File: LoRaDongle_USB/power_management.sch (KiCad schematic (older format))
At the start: 15 parts

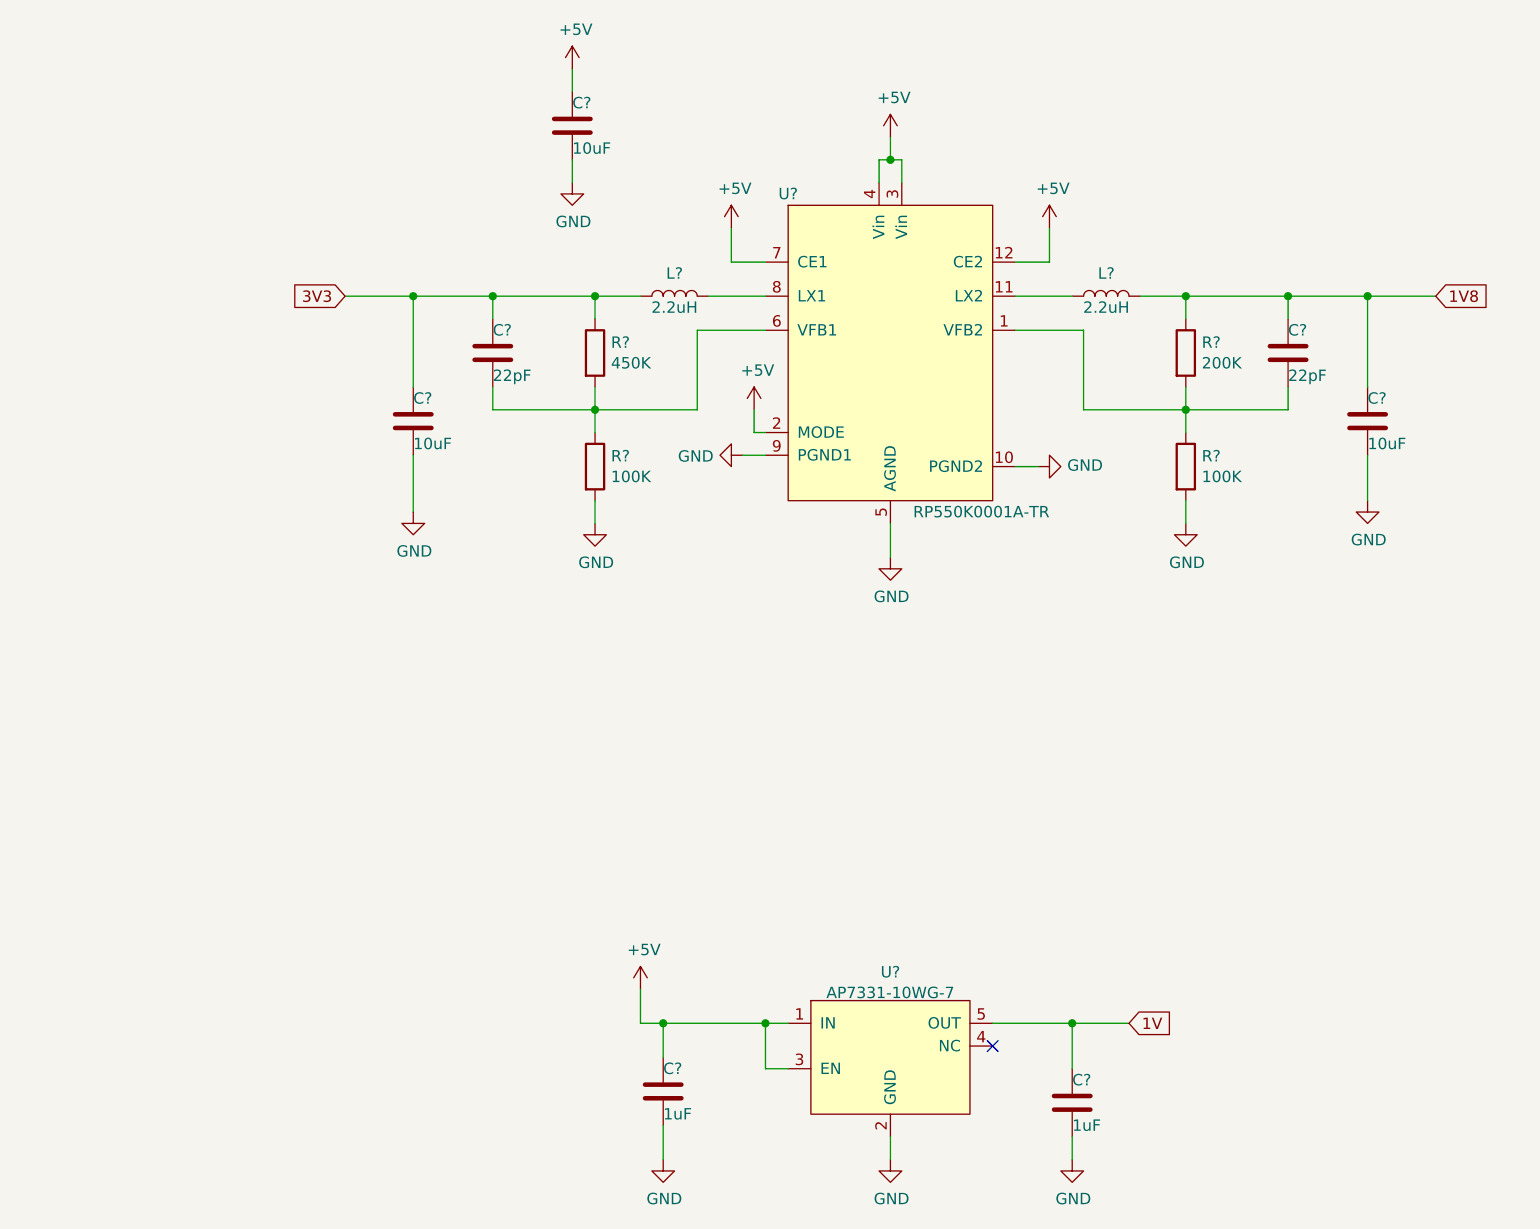
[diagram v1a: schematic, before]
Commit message: updated with dip switch
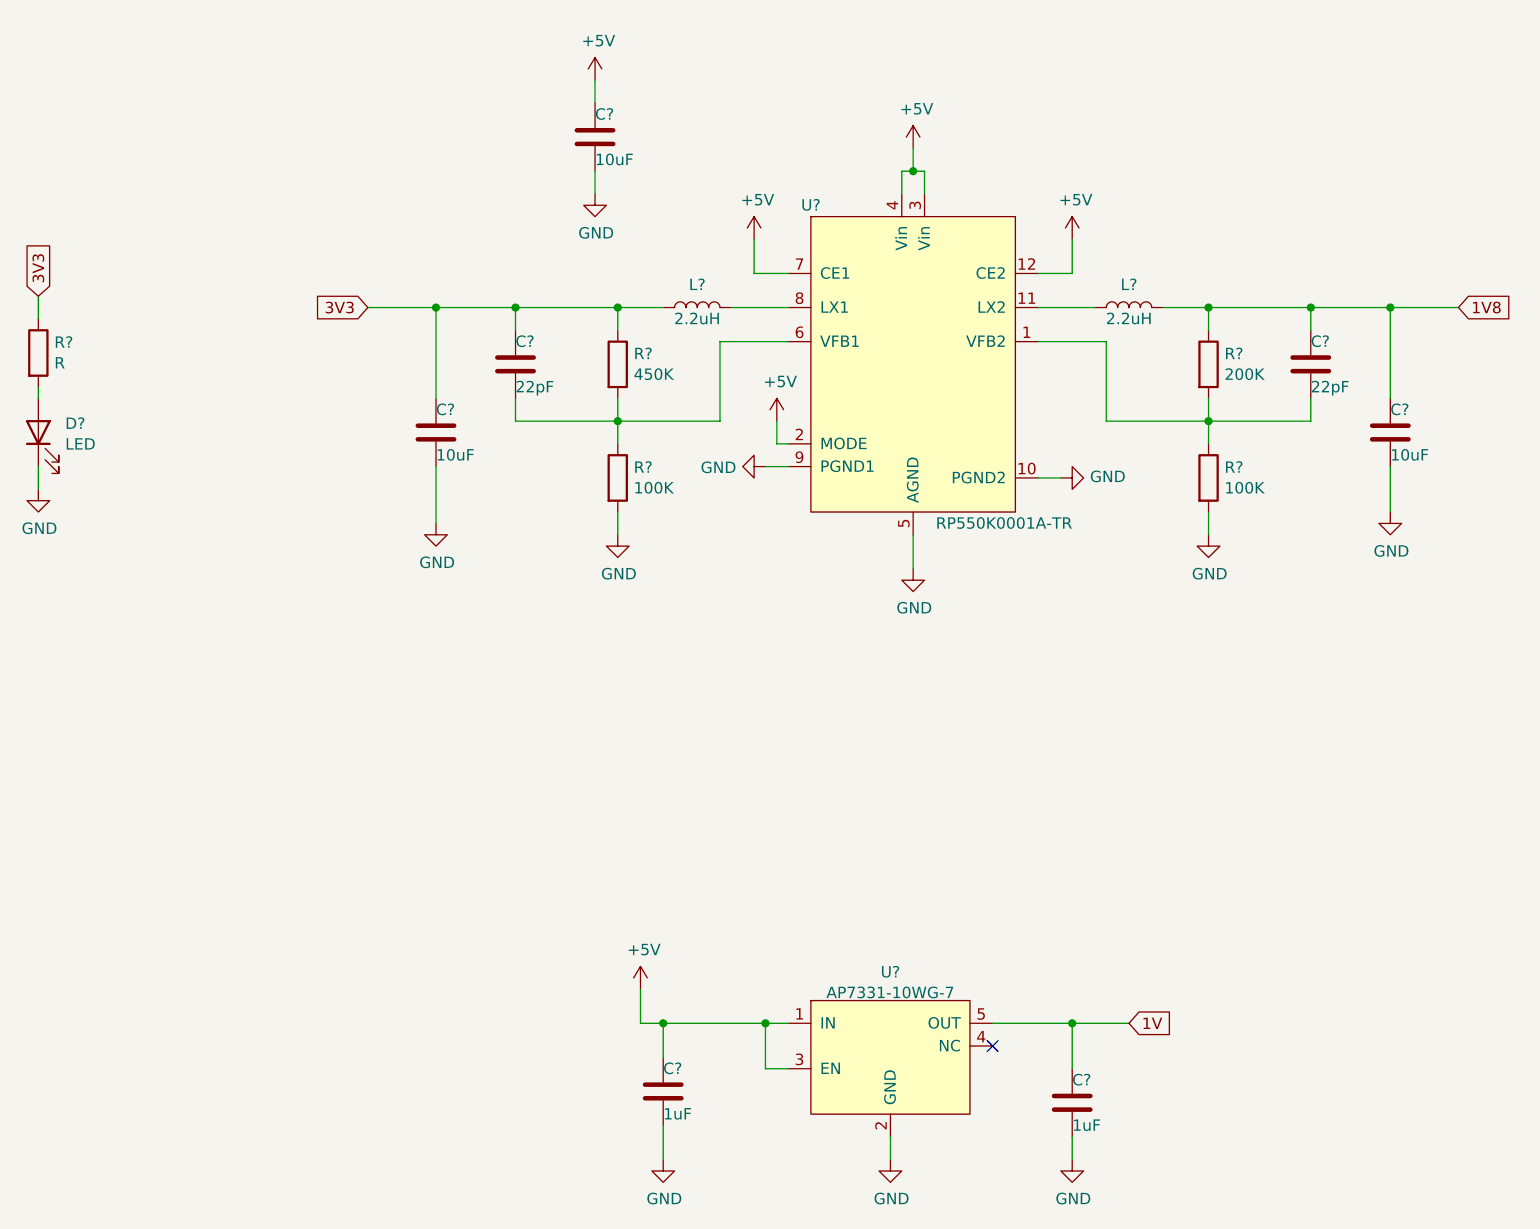
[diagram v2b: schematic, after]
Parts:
- added D?: LED, symbol Device:LED
- added R?: R, symbol Device:R
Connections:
- net 3V3: now also R?.1
- net GND: now also D?.1 (K)
- new net: D?.2 (A), R?.2
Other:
- moved on the sheet: C?, L?, R?, U?
